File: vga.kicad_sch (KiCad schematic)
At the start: 51 parts, among them J21 Audio Header, J22 DB15_Female_HighDensity_Mount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, J23 Audio Out, J24 Component A/V, J31 Conn_01x20, U43 74LVC374, U44 74LS374

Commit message: add footprints to differentiate 3.3V from 5V ICs
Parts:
- U43: footprint Package_DIP:DIP-20_W7.62mm -> snapeda:DIP-20_LVC_Family
- U44: footprint Package_DIP:DIP-20_W7.62mm -> snapeda:DIP-20_LS_Family
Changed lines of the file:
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@@
       (effects (font (size 1.27 1.27)) (justify left))
     )
-    (property "Footprint" "Package_DIP:DIP-20_W7.62mm" (id 2) (at 53.34 161.29 0)
+    (property "Footprint" "snapeda:DIP-20_LVC_Family" (id 2) (at 53.34 161.29 0)
       (effects (font (size 1.27 1.27)) hide)
     )
@@
       (effects (font (size 1.27 1.27)) (justify left))
     )
-    (property "Footprint" "Package_DIP:DIP-20_W7.62mm" (id 2) (at 109.22 161.29 0)
+    (property "Footprint" "snapeda:DIP-20_LS_Family" (id 2) (at 109.22 161.29 0)
       (effects (font (size 1.27 1.27)) hide)
     )

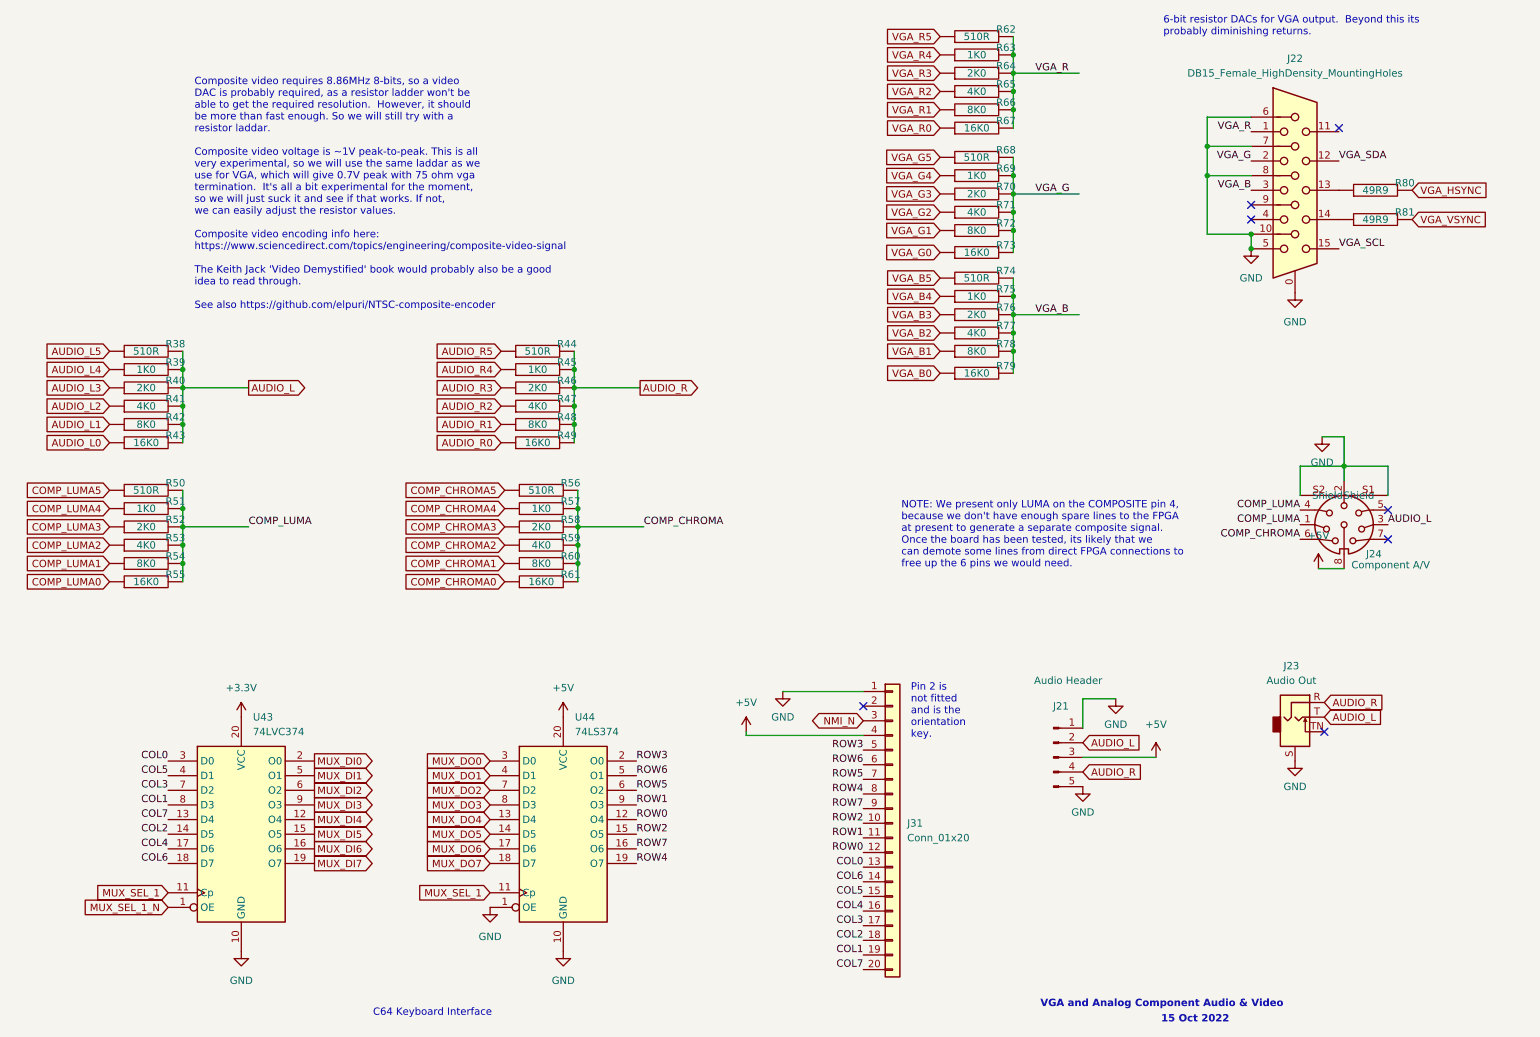
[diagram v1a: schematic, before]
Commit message: fix many DRC warnings
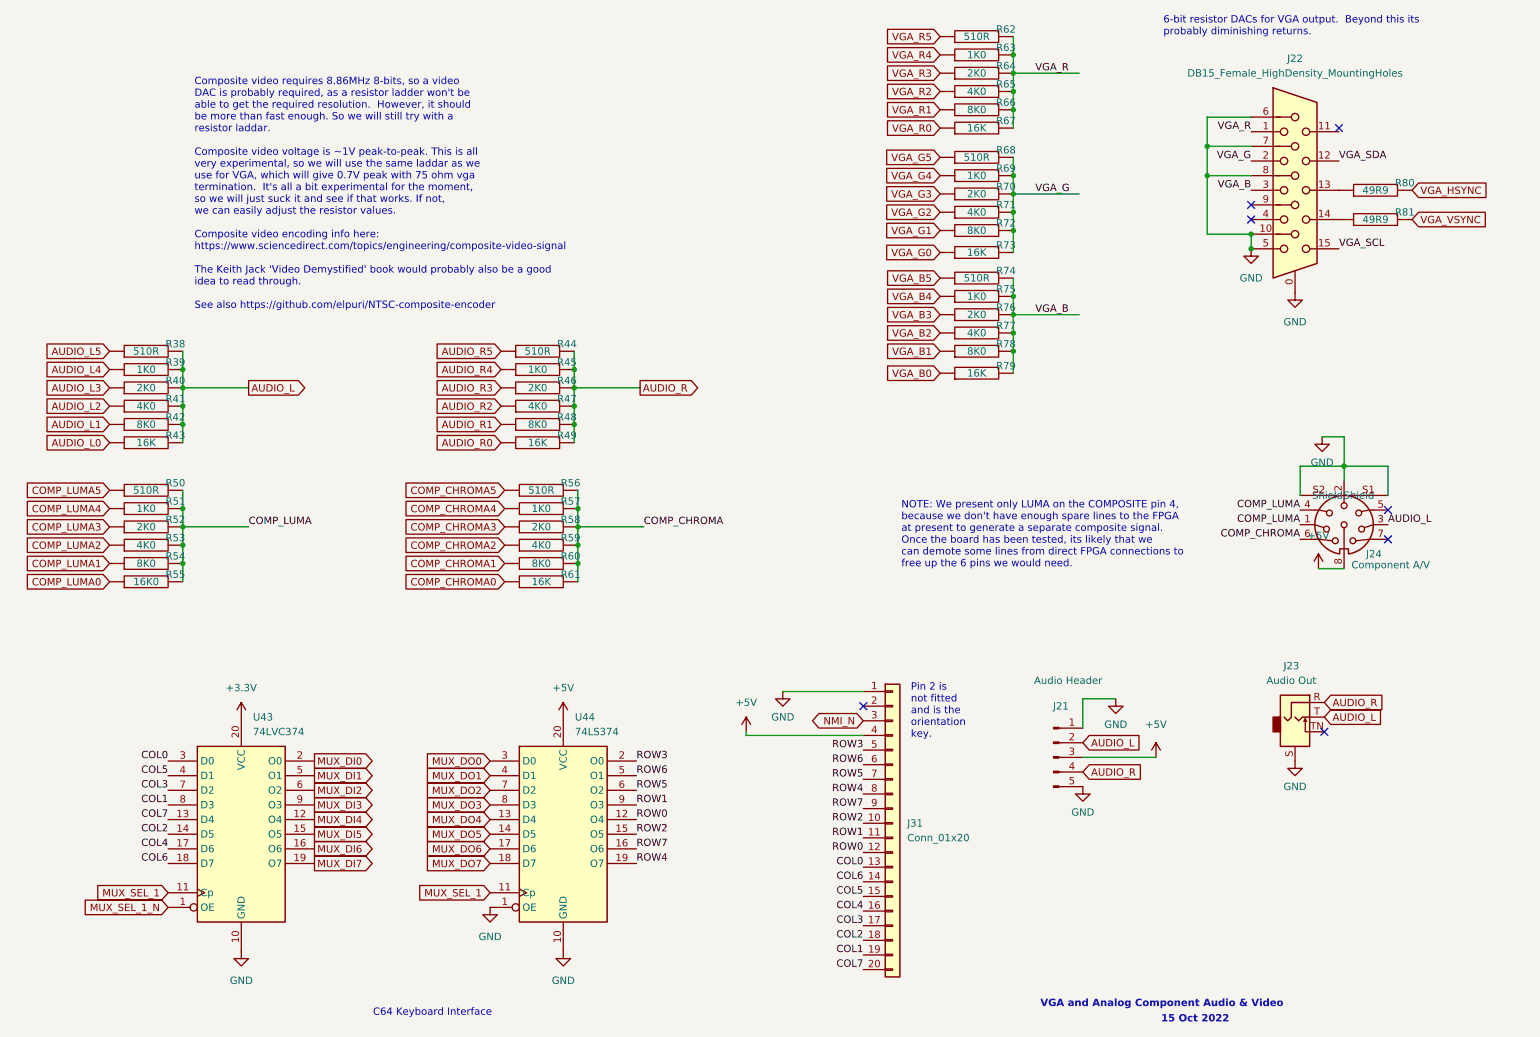
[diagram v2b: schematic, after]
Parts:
- R43, R49, R61, R67, R73, R79: value 16K0 -> 16K
- R80, R81: footprint Resistor_THT:R_Box_L8.4mm_W2.5mm_P5.08mm -> snapeda:Labeled Resistor
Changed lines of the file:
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@@
     (property "Reference" "R80" (id 0) (at 255.27 48.26 90))
     (property "Value" "49R9" (id 1) (at 250.19 49.53 90))
-    (property "Footprint" "Resistor_THT:R_Box_L8.4mm_W2.5mm_P5.08mm" (id 2) (at 250.19 49.53 0)
+    (property "Footprint" "snapeda:Labeled Resistor" (id 2) (at 250.19 49.53 0)
       (effects (font (size 1.27 1.27)) hide)
     )
@@
     (in_bom yes) (on_board yes)
     (property "Reference" "R73" (id 0) (at 186.055 59.055 90))
-    (property "Value" "16K0" (id 1) (at 180.975 60.325 90))
+    (property "Value" "16K" (id 1) (at 180.975 60.325 90))
     (property "Footprint" "snapeda:Labeled Resistor" (id 2) (at 180.975 60.325 0)
       (effects (font (size 1.27 1.27)) hide)
@@
     (in_bom yes) (on_board yes)
     (property "Reference" "R49" (id 0) (at 109.855 92.075 90))
-    (property "Value" "16K0" (id 1) (at 104.775 93.345 90))
+    (property "Value" "16K" (id 1) (at 104.775 93.345 90))
     (property "Footprint" "snapeda:Labeled Resistor" (id 2) (at 104.775 93.345 0)
       (effects (font (size 1.27 1.27)) hide)
@@
     (in_bom yes) (on_board yes)
     (property "Reference" "R43" (id 0) (at 41.91 92.075 90))
-    (property "Value" "16K0" (id 1) (at 36.83 93.345 90))
+    (property "Value" "16K" (id 1) (at 36.83 93.345 90))
     (property "Footprint" "snapeda:Labeled Resistor" (id 2) (at 36.83 93.345 0)
       (effects (font (size 1.27 1.27)) hide)
@@
     (in_bom yes) (on_board yes)
     (property "Reference" "R79" (id 0) (at 186.055 80.01 90))
-    (property "Value" "16K0" (id 1) (at 180.975 81.28 90))
+    (property "Value" "16K" (id 1) (at 180.975 81.28 90))
     (property "Footprint" "snapeda:Labeled Resistor" (id 2) (at 180.975 81.28 0)
       (effects (font (size 1.27 1.27)) hide)
@@
     (property "Reference" "R81" (id 0) (at 255.27 53.34 90))
     (property "Value" "49R9" (id 1) (at 250.19 54.61 90))
-    (property "Footprint" "Resistor_THT:R_Box_L8.4mm_W2.5mm_P5.08mm" (id 2) (at 250.19 54.61 0)
+    (property "Footprint" "snapeda:Labeled Resistor" (id 2) (at 250.19 54.61 0)
       (effects (font (size 1.27 1.27)) hide)
     )
@@
     (in_bom yes) (on_board yes)
     (property "Reference" "R61" (id 0) (at 110.49 116.205 90))
-    (property "Value" "16K0" (id 1) (at 105.41 117.475 90))
+    (property "Value" "16K" (id 1) (at 105.41 117.475 90))
     (property "Footprint" "snapeda:Labeled Resistor" (id 2) (at 105.41 117.475 0)
       (effects (font (size 1.27 1.27)) hide)
@@
     (in_bom yes) (on_board yes)
     (property "Reference" "R67" (id 0) (at 186.055 37.465 90))
-    (property "Value" "16K0" (id 1) (at 180.975 38.735 90))
+    (property "Value" "16K" (id 1) (at 180.975 38.735 90))
     (property "Footprint" "snapeda:Labeled Resistor" (id 2) (at 180.975 38.735 0)
       (effects (font (size 1.27 1.27)) hide)

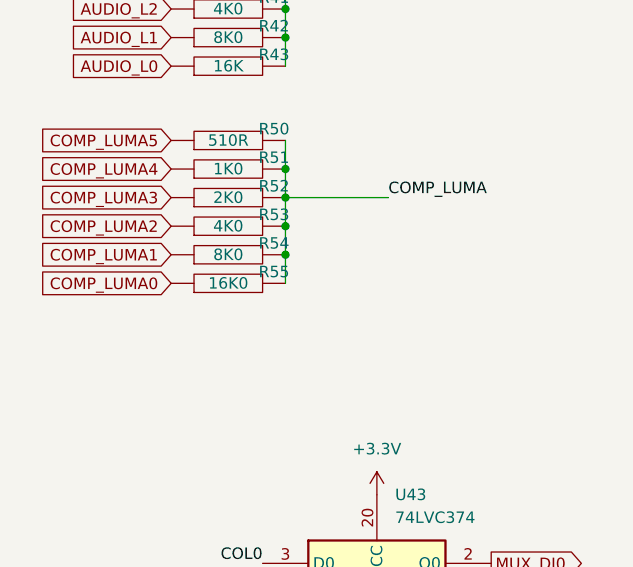
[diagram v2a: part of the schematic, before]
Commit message: re-do many labels and DRC fixes
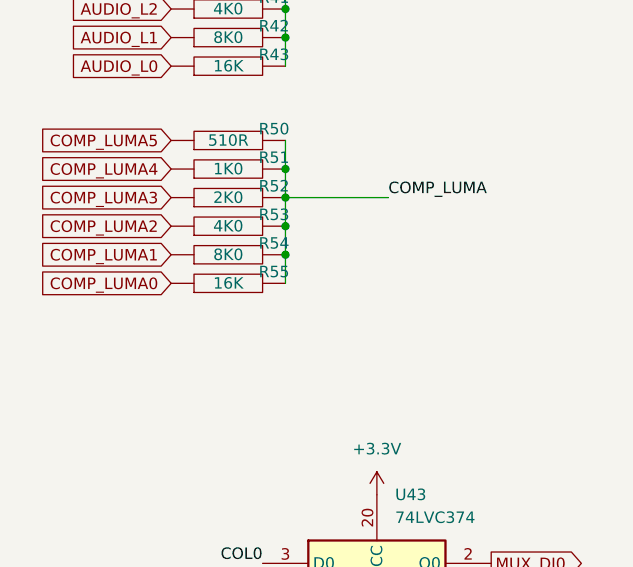
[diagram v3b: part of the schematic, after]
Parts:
- R55: value 16K0 -> 16K
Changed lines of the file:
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@@
     (in_bom yes) (on_board yes)
     (property "Reference" "R55" (id 0) (at 41.91 116.205 90))
-    (property "Value" "16K0" (id 1) (at 36.83 117.475 90))
+    (property "Value" "16K" (id 1) (at 36.83 117.475 90))
     (property "Footprint" "snapeda:Labeled Resistor" (id 2) (at 36.83 117.475 0)
       (effects (font (size 1.27 1.27)) hide)

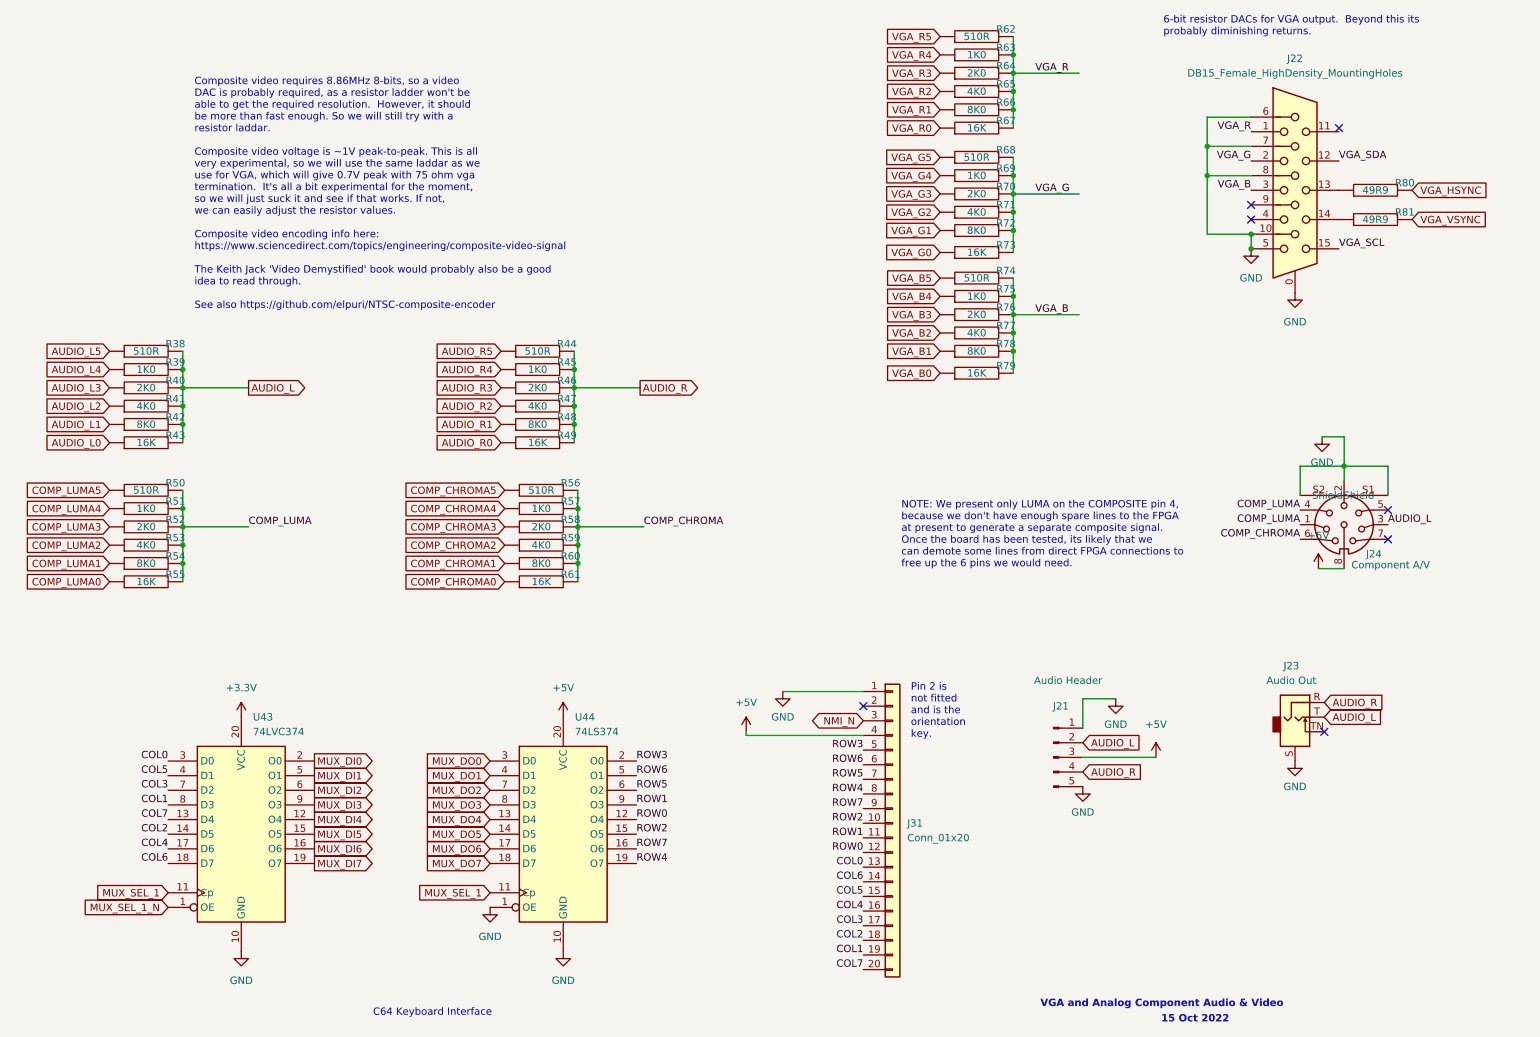
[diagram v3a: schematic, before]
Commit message: rework user port
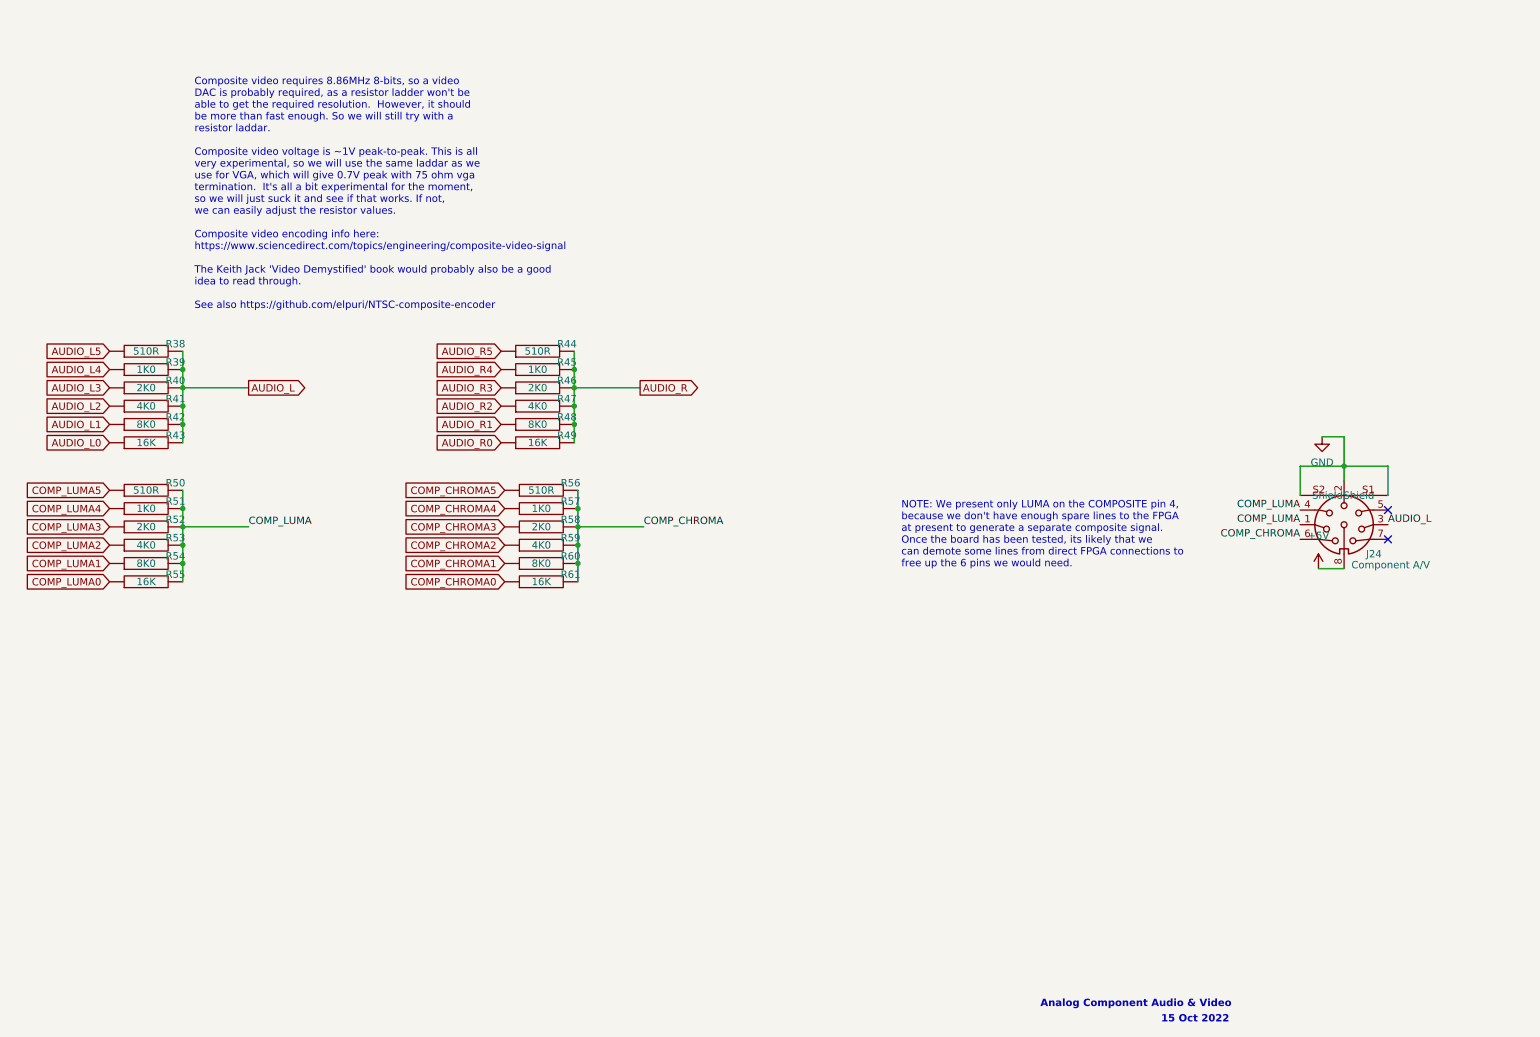
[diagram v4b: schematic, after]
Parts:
- removed J21: Audio Header, Connector_PinHeader_2.54mm:PinHeader_1x05_P2.54mm_Vertical, symbol Connector:Conn_01x05_Male
- removed J22: DB15_Female_HighDensity_MountingHoles, Connector_Dsub:DSUB-15-HD_Female_Horizontal_P2.29x1.98mm_EdgePinOffset8.35mm_Housed_MountingHolesOffset10.89mm, symbol Connector:DB15_Female_HighDensity_MountingHoles
- removed J23: Audio Out, Connector_Audio:Jack_3.5mm_CUI_SJ-3524-SMT_Horizontal, symbol 00Project-SDF-60J:3.5mm_Stereo_Audio_Jack STX-3500-4N
- removed J31: Conn_01x20, Connector_PinHeader_2.54mm:PinHeader_1x20_P2.54mm_Vertical, symbol Connector_Generic:Conn_01x20
- removed R62, R68, R74: 510R, snapeda:Labeled Resistor, symbol pspice:R
- removed R63, R69, R75: 1K0, snapeda:Labeled Resistor, symbol pspice:R
- removed R64, R70, R76: 2K0, snapeda:Labeled Resistor, symbol pspice:R
- removed R65, R71, R77: 4K0, snapeda:Labeled Resistor, symbol pspice:R
- removed R66, R72, R78: 8K0, snapeda:Labeled Resistor, symbol pspice:R
- removed R67, R73, R79: 16K, snapeda:Labeled Resistor, symbol pspice:R
- removed R80, R81: 49R9, snapeda:Labeled Resistor, symbol pspice:R
- removed U43: 74LVC374, snapeda:DIP-20_LVC_Family, symbol 74xx:74HC374
- removed U44: 74LS374, snapeda:DIP-20_LS_Family, symbol 74xx:74LS374
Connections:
- no-connect marks 7 -> 2
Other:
- note added: "Analog Component Audio & Video"
- note removed: "6-bit resistor DACs for VGA output. Beyond this its probably diminishing returns."
- note removed: "C64 Keyboard Interface"
- note removed: "Pin 2 is not fitted and is the orientation key."
- note removed: "VGA and Analog Component Audio & Video"
